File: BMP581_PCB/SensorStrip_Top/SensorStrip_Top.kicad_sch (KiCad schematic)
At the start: 7 parts

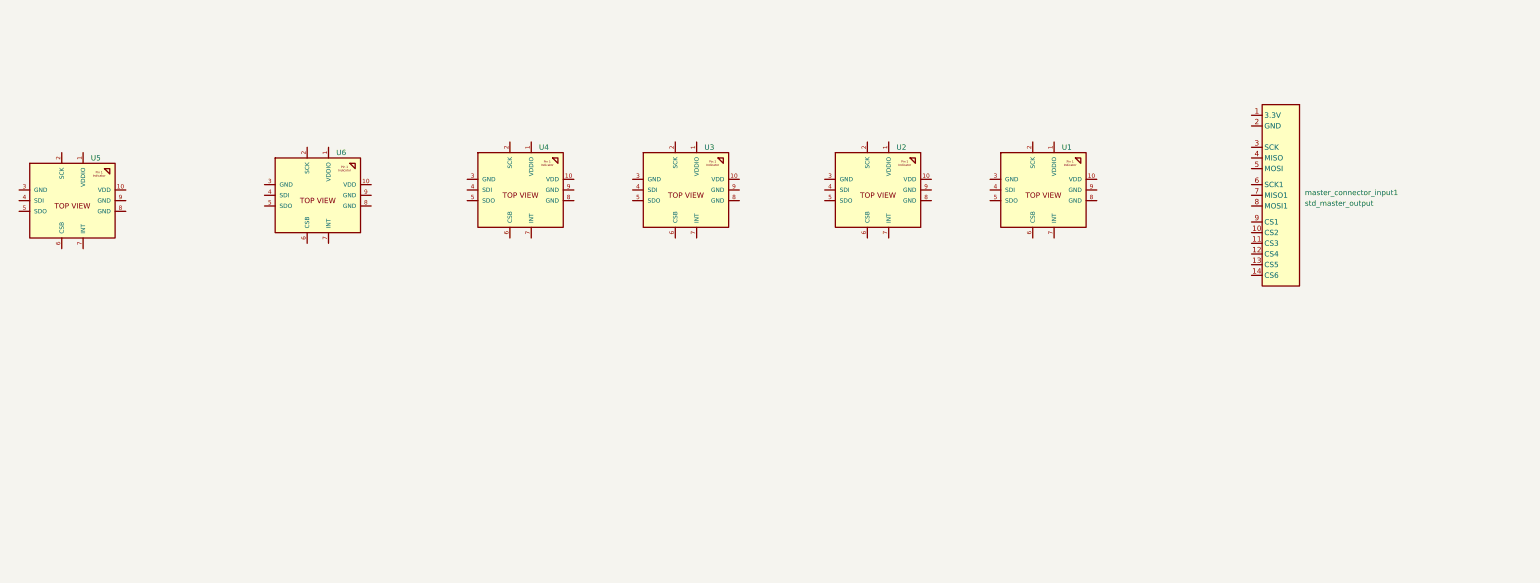
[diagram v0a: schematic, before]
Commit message: New footprint submodule + progress
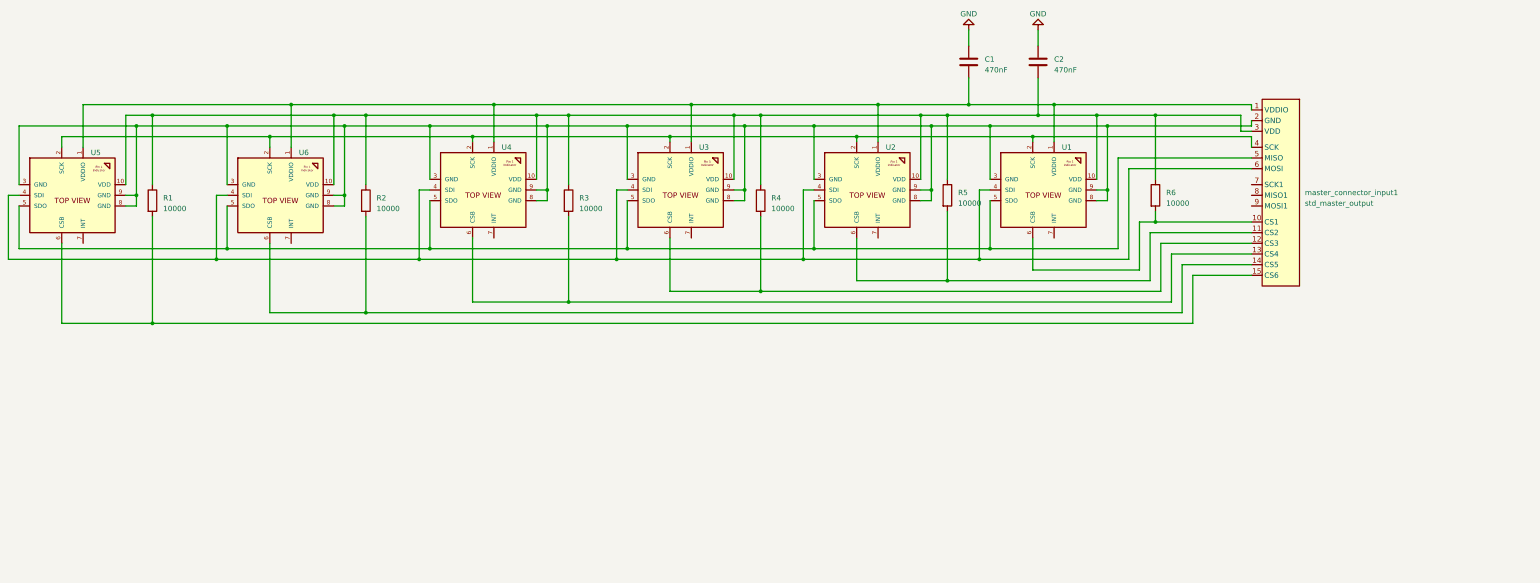
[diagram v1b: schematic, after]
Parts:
- added C1, C2: 470nF, Capacitor_SMD:C_0603_1608Metric, symbol Device:C
- added R1, R2, R3, R4, R5, R6: 10000, Resistor_SMD:R_0201_0603Metric, symbol Device:R
- U1, U2, U3, U4, U5, U6: footprint BMP581 -> BMP581:BMP581_Landing_Pattern
- master_connector_input1: footprint (none) -> Connector_PinHeader_1.00mm:PinHeader_1x15_P1.00mm_Vertical_SMD_Pin1Right
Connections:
- net at U2.1 (VDDIO): now also U1.1 (VDDIO), U3.1 (VDDIO), U4.1 (VDDIO), U5.1 (VDDIO), U6.1 (VDDIO), master_connector_input1.1 (VDDIO), C1.2
- net at U2.10 (VDD): now also U1.10 (VDD), U3.10 (VDD), U4.10 (VDD), U5.10 (VDD), U6.10 (VDD), master_connector_input1.3 (VDD), C2.2, R1.1, R2.1, R3.1, R4.1, R5.1, R6.1
- net at U2.2 (SCK): now also U1.2 (SCK), U3.2 (SCK), U4.2 (SCK), U5.2 (SCK), U6.2 (SCK), master_connector_input1.4 (SCK)
- net at U2.3 (GND): now also U1.3 (GND), U1.8 (GND), U1.9 (GND), U2.8 (GND), U2.9 (GND), U3.3 (GND), U3.8 (GND), U3.9 (GND), U4.3 (GND), U4.8 (GND), U4.9 (GND), U5.3 (GND), U5.8 (GND), U5.9 (GND), U6.3 (GND), U6.8 (GND), U6.9 (GND), master_connector_input1.2 (GND)
- net at U2.4 (SDI): now also U1.4 (SDI), U3.4 (SDI), U4.4 (SDI), U5.4 (SDI), U6.4 (SDI), master_connector_input1.6 (MOSI)
- net at U2.5 (SDO): now also U1.5 (SDO), U3.5 (SDO), U4.5 (SDO), U5.5 (SDO), U6.5 (SDO), master_connector_input1.5 (MISO)
- net at U2.6 (CSB): now also master_connector_input1.11 (CS2), R5.2
- net at U4.6 (CSB): now also master_connector_input1.13 (CS4), R3.2
- net at U3.6 (CSB): now also master_connector_input1.12 (CS3), R4.2
- net at U1.6 (CSB): now also master_connector_input1.10 (CS1), R6.2
- net at master_connector_input1.14 (CS5): now also U6.6 (CSB), R2.2
- net at U5.6 (CSB): now also master_connector_input1.15 (CS6), R1.2
- new net GND: C1.1, C2.1
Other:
- moved on the sheet: U2, U3, U4, U5, U6

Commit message: update strips
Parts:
- R1, R2, R3, R4, R5, R6: footprint Resistor_SMD:R_0201_0603Metric -> Resistor_SMD:R_0402_1005Metric
- TopConnector1: renamed from master_connector_input1; footprint Connector_PinHeader_1.00mm:PinHeader_1x15_P1.00mm_Vertical_SMD_Pin1Right -> BMP581:Strip_pins_top
- renumbered U5 to U1, U6 to U2, U4 to U3, U3 to U4, U2 to U5, U1 to U6
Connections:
- net GND: now also TopConnector1.2 (GND), U1.3 (GND), U1.8 (GND), U1.9 (GND), U2.3 (GND), U2.8 (GND), U2.9 (GND), U3.3 (GND), U3.8 (GND), U3.9 (GND), U4.3 (GND), U4.8 (GND), U4.9 (GND), U5.3 (GND), U5.8 (GND), U5.9 (GND), U6.3 (GND), U6.8 (GND), U6.9 (GND)

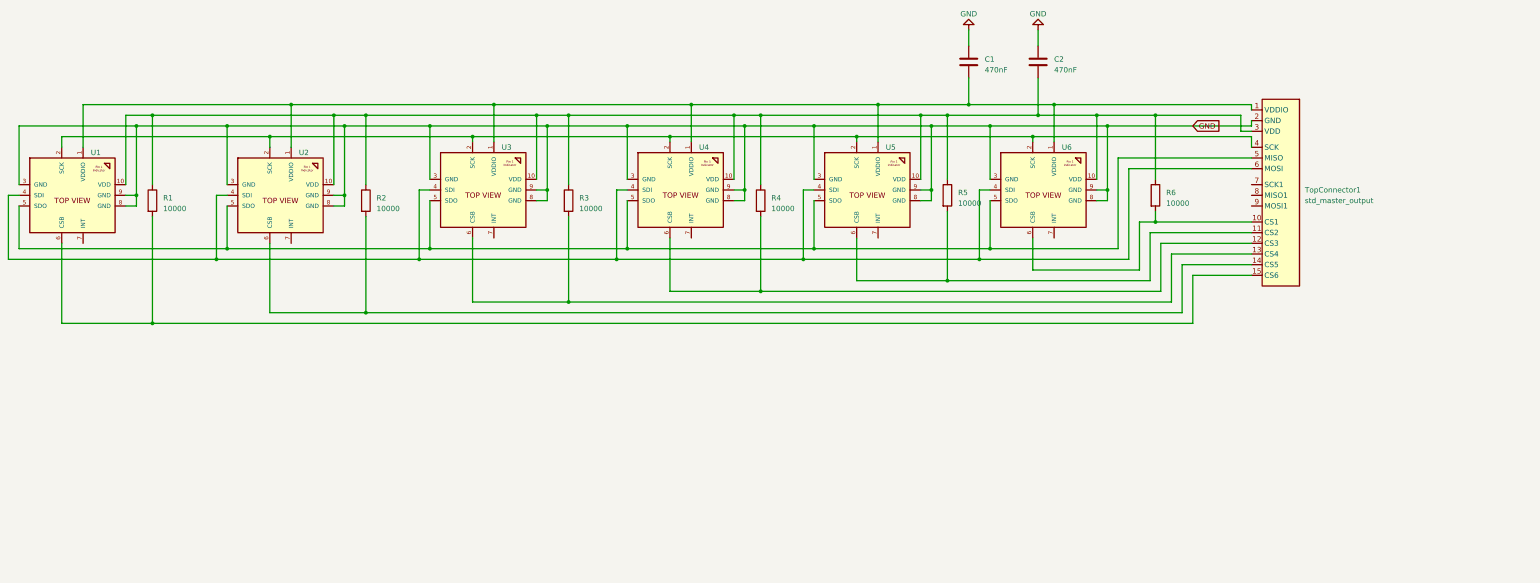
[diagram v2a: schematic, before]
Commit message: Top sensor strip completed v1
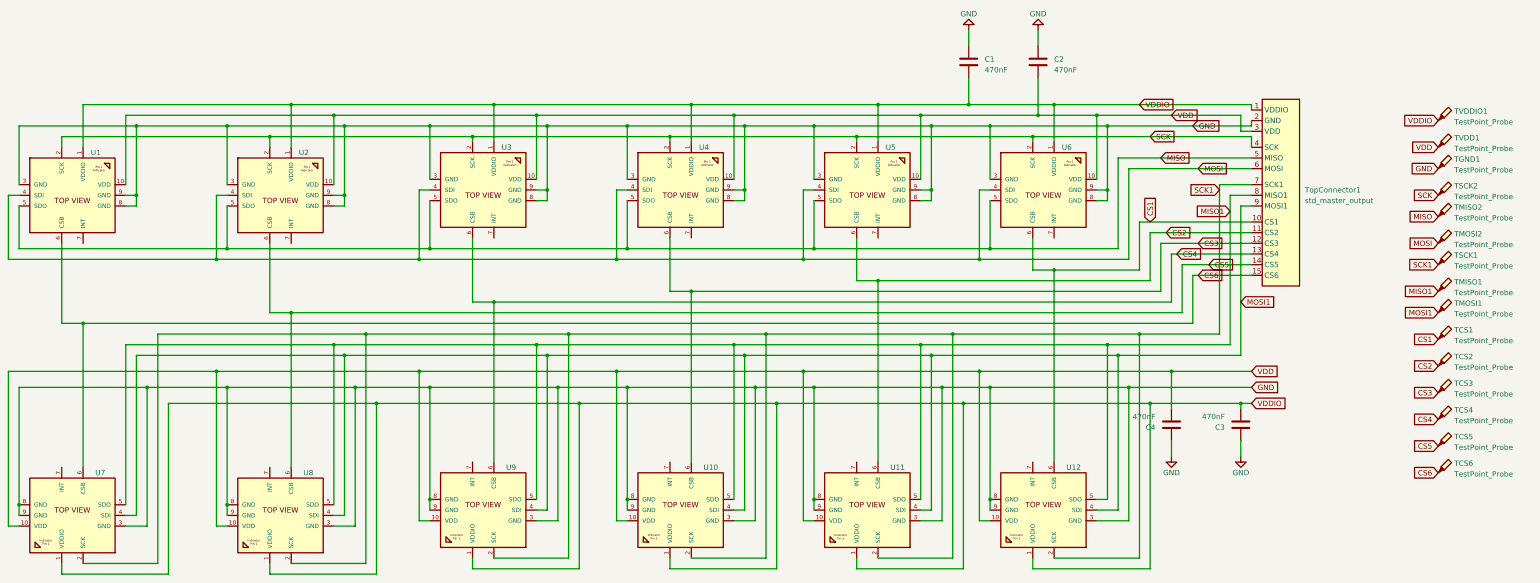
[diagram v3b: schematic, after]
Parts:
- removed R1, R2, R3, R4, R5, R6: 10000, Resistor_SMD:R_0402_1005Metric, symbol Device:R
- added C3, C4: 470nF, Capacitor_SMD:C_0603_1608Metric, symbol Device:C
- added TCS1, TCS2, TCS3, TCS4, TCS5, TCS6, TGND1, TMISO1, TMISO2, TMOSI1, TMOSI2, TSCK1, TSCK2, TVDD1, TVDDIO1: TestPoint_Probe, TestPoint:TestPoint_Pad_1.0x1.0mm, symbol Connector:TestPoint_Probe
- added U10, U11, U12, U7, U8, U9: ~, BMP581:BMP581_Landing_Pattern, symbol BMP581_symbol:BMP581
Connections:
- net GND: now also C3.1, C4.1, TGND1.1, U10.3 (GND), U10.8 (GND), U10.9 (GND), U11.3 (GND), U11.8 (GND), U11.9 (GND), U12.3 (GND), U12.8 (GND), U12.9 (GND), U7.3 (GND), U7.8 (GND), U7.9 (GND), U8.3 (GND), U8.8 (GND), U8.9 (GND), U9.3 (GND), U9.8 (GND), U9.9 (GND)
- net VDDIO: now reaches C1.2, TopConnector1.1 (VDDIO), U1.1 (VDDIO), U2.1 (VDDIO), U3.1 (VDDIO), U4.1 (VDDIO), U5.1 (VDDIO), U6.1 (VDDIO)
- net VDDIO: now also C3.2, TVDDIO1.1, U10.1 (VDDIO), U11.1 (VDDIO), U12.1 (VDDIO), U7.1 (VDDIO), U8.1 (VDDIO), U9.1 (VDDIO)
- net VDD: now reaches C2.2, TopConnector1.3 (VDD), U1.10 (VDD), U2.10 (VDD), U3.10 (VDD), U4.10 (VDD), U5.10 (VDD), U6.10 (VDD)
- net VDD: now also C4.2, TVDD1.1, U10.10 (VDD), U11.10 (VDD), U12.10 (VDD), U7.10 (VDD), U8.10 (VDD), U9.10 (VDD)
- net SCK: now reaches TopConnector1.4 (SCK), U1.2 (SCK), U2.2 (SCK), U3.2 (SCK), U4.2 (SCK), U5.2 (SCK), U6.2 (SCK)
- net SCK: now also TSCK2.1
- net MOSI: now reaches TopConnector1.6 (MOSI), U1.4 (SDI), U2.4 (SDI), U3.4 (SDI), U4.4 (SDI), U5.4 (SDI), U6.4 (SDI)
- net MOSI: now also TMOSI2.1
- net MISO: now reaches TopConnector1.5 (MISO), U1.5 (SDO), U2.5 (SDO), U3.5 (SDO), U4.5 (SDO), U5.5 (SDO), U6.5 (SDO)
- net MISO: now also TMISO2.1
- net CS2: now reaches TopConnector1.11 (CS2), U5.6 (CSB)
- net CS2: now also TCS2.1, U11.6 (CSB)
- net CS4: now reaches TopConnector1.13 (CS4), U3.6 (CSB)
- net CS4: now also TCS4.1, U9.6 (CSB)
- net CS6: now reaches TopConnector1.15 (CS6), U1.6 (CSB)
- net CS6: now also TCS6.1, U7.6 (CSB)
- net CS5: now reaches TopConnector1.14 (CS5), U2.6 (CSB)
- net CS5: now also TCS5.1, U8.6 (CSB)
- net CS3: now reaches TopConnector1.12 (CS3), U4.6 (CSB)
- net CS3: now also TCS3.1, U10.6 (CSB)
- net CS1: now reaches TopConnector1.10 (CS1), U6.6 (CSB)
- net CS1: now also TCS1.1, U12.6 (CSB)
- net SCK1: now reaches TopConnector1.7 (SCK1)
- net SCK1: now also TSCK1.1, U10.2 (SCK), U11.2 (SCK), U12.2 (SCK), U7.2 (SCK), U8.2 (SCK), U9.2 (SCK)
- net MISO1: now reaches TopConnector1.8 (MISO1)
- net MISO1: now also TMISO1.1, U10.5 (SDO), U11.5 (SDO), U12.5 (SDO), U7.5 (SDO), U8.5 (SDO), U9.5 (SDO)
- net MOSI1: now reaches TopConnector1.9 (MOSI1)
- net MOSI1: now also TMOSI1.1, U10.4 (SDI), U11.4 (SDI), U12.4 (SDI), U7.4 (SDI), U8.4 (SDI), U9.4 (SDI)
